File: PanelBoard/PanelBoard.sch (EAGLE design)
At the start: 8 parts, among them K1 ARK500/2, K2 ARK500/2, K3 ARK500/2, K4 ARK500/2

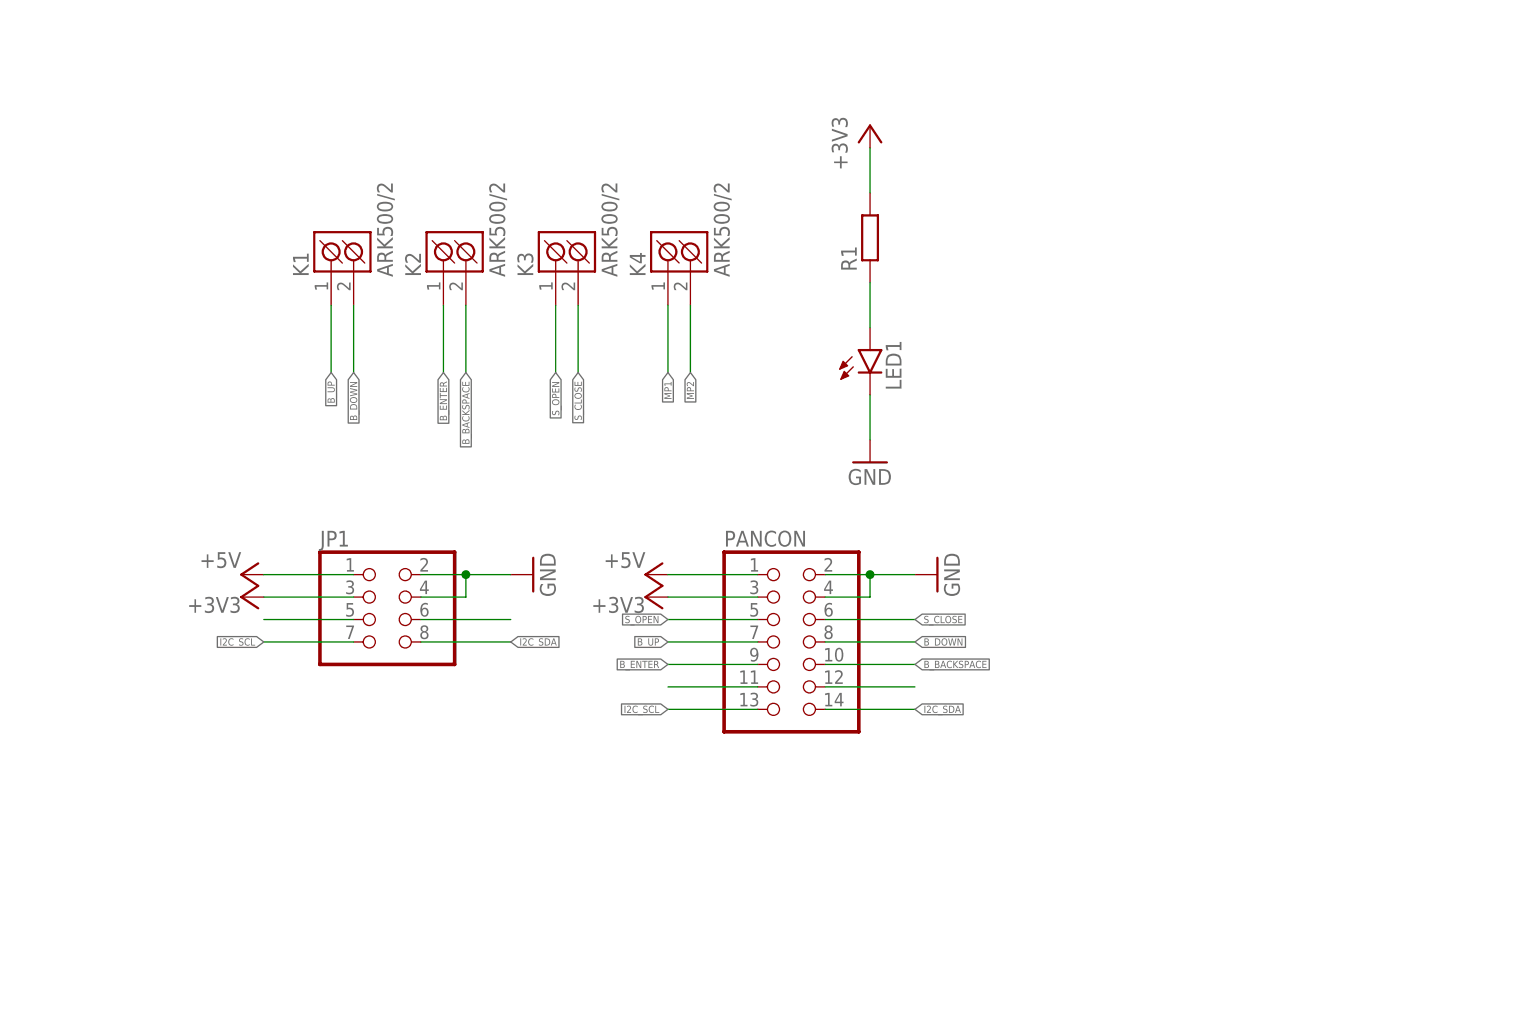
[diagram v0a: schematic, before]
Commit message: PanelBoard layout reworked
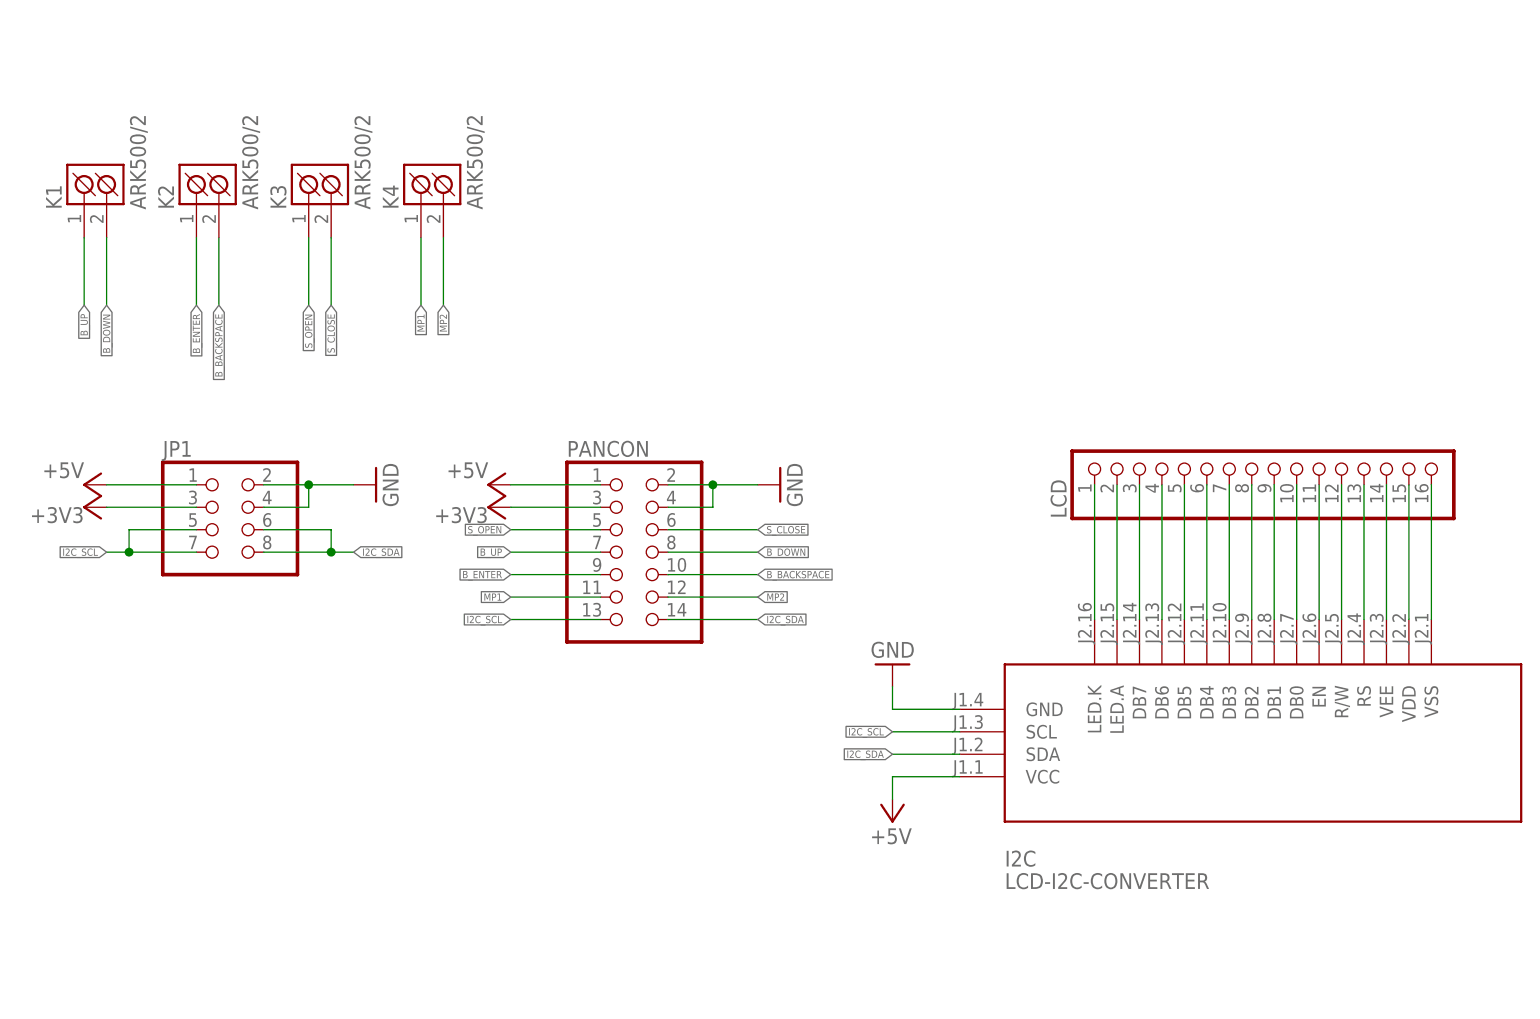
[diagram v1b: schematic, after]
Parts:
- removed LED1: (no value), led:LEDCHIPLED_0603
- removed R1: (no value), rcl:R-EU_R0603
- added I2C: LCD-I2C-CONVERTER, diy-modules:LCD-I2C-CONVERTER
- added LCD: (no value), pinhead:PINHD-1X16
- JP1: device pinhead:PINHD-2X4 -> pinhead:PINHD-2X4/90
- PANCON: device pinhead:PINHD-2X7 -> pinhead:PINHD-2X7/90
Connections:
- removed net N$1: JP1.5
- removed net N$2: JP1.6
- removed net N$4: LED1.A, R1.1
- removed net N$8: PANCON.11
- removed net N$9: PANCON.12
- new net N$10: I2C.DB5, LCD.5
- new net N$11: I2C.DB4, LCD.6
- new net N$12: I2C.DB3, LCD.7
- new net N$13: I2C.DB2, LCD.8
- new net N$14: I2C.DB1, LCD.9
- new net N$15: I2C.DB0, LCD.10
- new net N$16: I2C.EN, LCD.11
- new net N$17: I2C.R/W, LCD.12
- new net N$18: I2C.RS, LCD.13
- new net N$19: I2C.VEE, LCD.14
- new net N$20: I2C.VDD, LCD.15
- new net N$21: I2C.VSS, LCD.16
- new net N$3: I2C.LED.K, LCD.1
- new net N$5: I2C.LED.A, LCD.2
- new net N$6: I2C.DB7, LCD.3
- new net N$7: I2C.DB6, LCD.4
- net +3V3: no longer R1.2
- net +5V: now also I2C.VCC
- net GND: now also I2C.GND; no longer LED1.C
- net I2C_SCL: now also I2C.SCL, JP1.5
- net I2C_SDA: now also I2C.SDA, JP1.6
- net MP1: now also PANCON.11
- net MP2: now also PANCON.12
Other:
- moved on the sheet: JP1, K1, K2, K3, K4, PANCON

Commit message: Improved schematics layout.
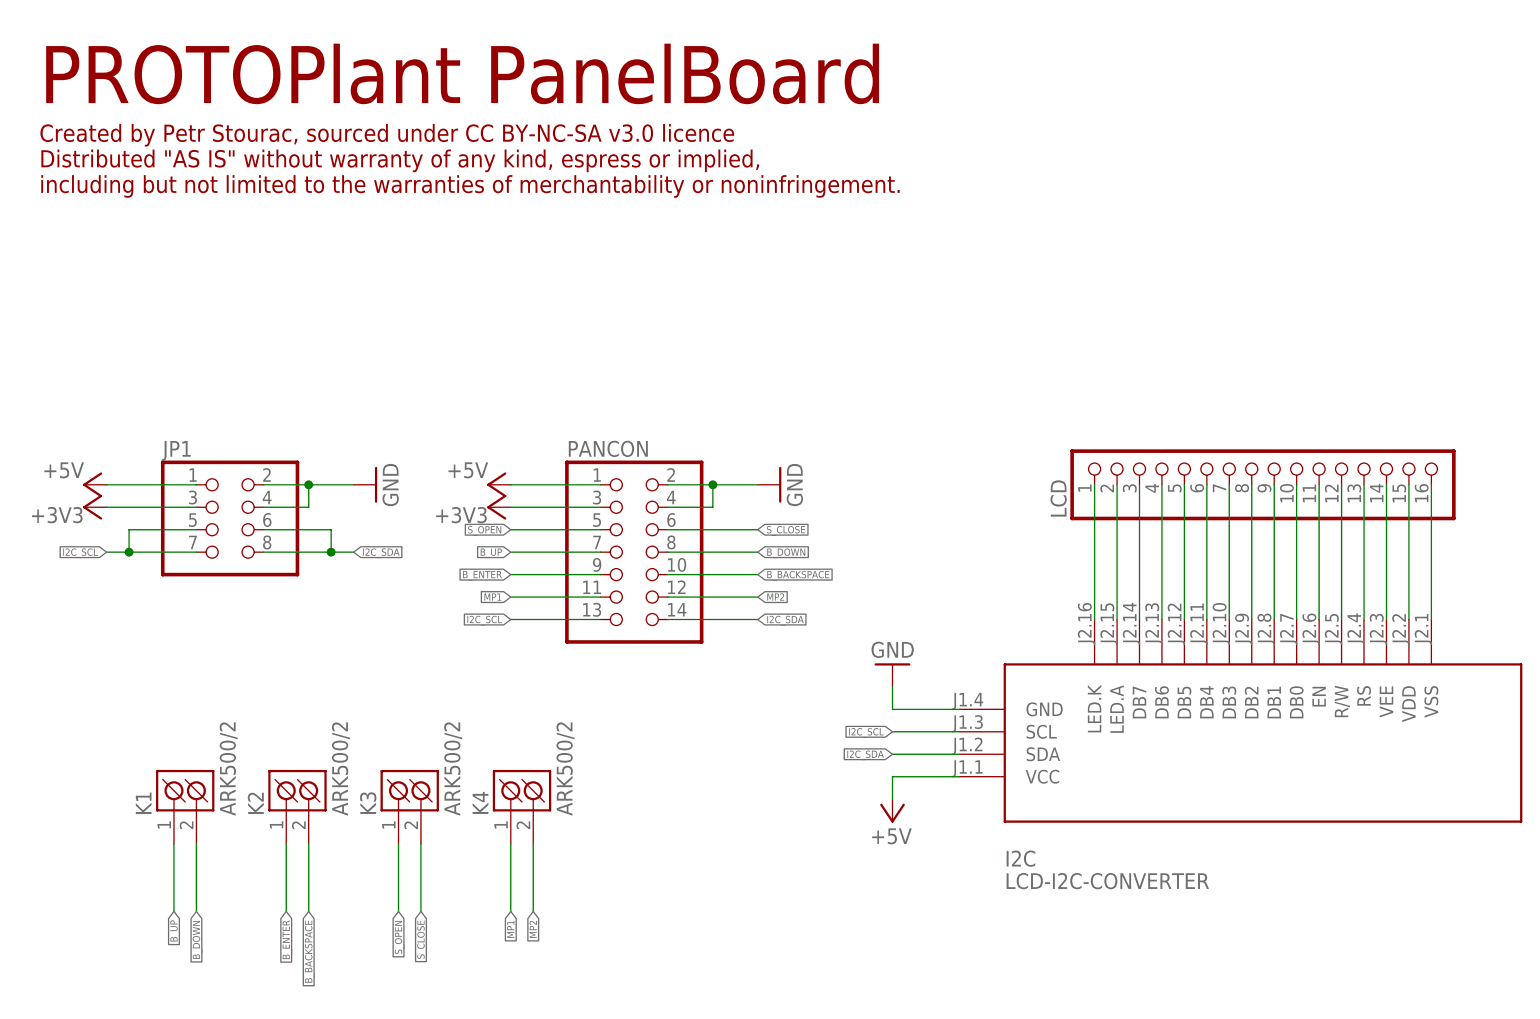
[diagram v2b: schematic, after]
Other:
- note added: "Created by Petr Stourac, sourced under CC BY-NC-SA v3.0 licence Distributed "AS IS" without warranty of any kind, espress or implied, including but not limited to the warranties of merchantability or noninfringement."
- note added: "PROTOPlant PanelBoard"
- moved on the sheet: K1, K2, K3, K4
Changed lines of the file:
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@@
 <?xml version="1.0" encoding="utf-8"?>
 <!DOCTYPE eagle SYSTEM "eagle.dtd">
-<eagle version="9.5.2">
+<eagle version="9.6.1">
 <drawing>
 <settings>
@@
 <setting verticaltext="up"/>
 </settings>
-<grid distance="0.1" unitdist="inch" unit="inch" style="lines" multiple="1" display="no" altdistance="0.01" altunitdist="inch" altunit="inch"/>
+<grid distance="0.1" unitdist="inch" unit="inch" style="lines" multiple="1" display="yes" altdistance="0.01" altunitdist="inch" altunit="inch"/>
 <layers>
 <layer number="1" name="Top" color="4" fill="1" visible="no" active="no"/>
@@
 <parts>
 <part name="FRAME1" library="frames" library_urn="urn:adsk.eagle:library:229" deviceset="A5L-LOC" device=""/>
-<part name="K1" library="#PaJa_konektory" deviceset="ARK500/2" device=""/>
-<part name="K2" library="#PaJa_konektory" deviceset="ARK500/2" device=""/>
-<part name="K3" library="#PaJa_konektory" deviceset="ARK500/2" device=""/>
-<part name="K4" library="#PaJa_konektory" deviceset="ARK500/2" device=""/>
+<part name="K1" library="#PaJa_konektory" library_urn="urn:adsk.eagle:library:19754563" deviceset="ARK500/2" device="" package3d_urn="urn:adsk.eagle:package:19754484/4"/>
+<part name="K2" library="#PaJa_konektory" library_urn="urn:adsk.eagle:library:19754563" deviceset="ARK500/2" device="" package3d_urn="urn:adsk.eagle:package:19754484/4"/>
+<part name="K3" library="#PaJa_konektory" library_urn="urn:adsk.eagle:library:19754563" deviceset="ARK500/2" device="" package3d_urn="urn:adsk.eagle:package:19754484/4"/>
+<part name="K4" library="#PaJa_konektory" library_urn="urn:adsk.eagle:library:19754563" deviceset="ARK500/2" device="" package3d_urn="urn:adsk.eagle:package:19754484/4"/>
 <part name="JP1" library="pinhead" library_urn="urn:adsk.eagle:library:325" deviceset="PINHD-2X4" device="/90" package3d_urn="urn:adsk.eagle:package:22465/2"/>
 <part name="PANCON" library="pinhead" library_urn="urn:adsk.eagle:library:325" deviceset="PINHD-2X7" device="/90" package3d_urn="urn:adsk.eagle:package:22479/2"/>
@@
 <sheet>
 <plain>
+<text x="7.62" y="119.38" size="6.4516" layer="94">PROTOPlant PanelBoard</text>
+<text x="7.62" y="109.22" size="1.9304" layer="94">Created by Petr Stourac, sourced under CC BY-NC-SA v3.0 licence
+Distributed "AS IS" without warranty of any kind, espress or implied,
+including but not limited to the warranties of merchantability or noninfringement.</text>
 </plain>
 <instances>
@@
 <attribute name="SHEET" x="154.305" y="5.08" size="2.54" layer="94"/>
 </instance>
-<instance part="K1" gate="K" x="12.7" y="109.22" smashed="yes" rot="R90">
-<attribute name="NAME" x="10.161" y="107.3335" size="1.778" layer="95" rot="R90"/>
-<attribute name="VALUE" x="19.679" y="107.3335" size="1.778" layer="96" rot="R90"/>
-</instance>
-<instance part="K2" gate="K" x="25.4" y="109.22" smashed="yes" rot="R90">
-<attribute name="NAME" x="22.861" y="107.3335" size="1.778" layer="95" rot="R90"/>
-<attribute name="VALUE" x="32.379" y="107.3335" size="1.778" layer="96" rot="R90"/>
-</instance>
-<instance part="K3" gate="K" x="38.1" y="109.22" smashed="yes" rot="R90">
-<attribute name="NAME" x="35.561" y="107.3335" size="1.778" layer="95" rot="R90"/>
-<attribute name="VALUE" x="45.079" y="107.3335" size="1.778" layer="96" rot="R90"/>
-</instance>
-<instance part="K4" gate="K" x="50.8" y="109.22" smashed="yes" rot="R90">
-<attribute name="NAME" x="48.261" y="107.3335" size="1.778" layer="95" rot="R90"/>
-<attribute name="VALUE" x="57.779" y="107.3335" size="1.778" layer="96" rot="R90"/>
+<instance part="K1" gate="K" x="22.86" y="40.64" smashed="yes" rot="R90">
+<attribute name="NAME" x="20.321" y="38.7535" size="1.778" layer="95" rot="R90"/>
+<attribute name="VALUE" x="29.839" y="38.7535" size="1.778" layer="96" rot="R90"/>
+</instance>
+<instance part="K2" gate="K" x="35.56" y="40.64" smashed="yes" rot="R90">
+<attribute name="NAME" x="33.021" y="38.7535" size="1.778" layer="95" rot="R90"/>
+<attribute name="VALUE" x="42.539" y="38.7535" size="1.778" layer="96" rot="R90"/>
+</instance>
+<instance part="K3" gate="K" x="48.26" y="40.64" smashed="yes" rot="R90">
+<attribute name="NAME" x="45.721" y="38.7535" size="1.778" layer="95" rot="R90"/>
+<attribute name="VALUE" x="55.239" y="38.7535" size="1.778" layer="96" rot="R90"/>
+</instance>
+<instance part="K4" gate="K" x="60.96" y="40.64" smashed="yes" rot="R90">
+<attribute name="NAME" x="58.421" y="38.7535" size="1.778" layer="95" rot="R90"/>
+<attribute name="VALUE" x="67.939" y="38.7535" size="1.778" layer="96" rot="R90"/>
 </instance>
 <instance part="JP1" gate="A" x="27.94" y="71.12" smashed="yes">
@@
 <segment>
 <pinref part="K1" gate="K" pin="K1"/>
-<wire x1="12.7" y1="104.14" x2="12.7" y2="96.52" width="0.1524" layer="91"/>
-<label x="12.7" y="96.52" size="0.8128" layer="95" rot="R270" xref="yes"/>
+<wire x1="22.86" y1="35.56" x2="22.86" y2="27.94" width="0.1524" layer="91"/>
+<label x="22.86" y="27.94" size="0.8128" layer="95" rot="R270" xref="yes"/>
 </segment>
 <segment>
@@
 <segment>
 <pinref part="K1" gate="K" pin="K2"/>
-<wire x1="15.24" y1="104.14" x2="15.24" y2="96.52" width="0.1524" layer="91"/>
-<label x="15.24" y="96.52" size="0.8128" layer="95" rot="R270" xref="yes"/>
+<wire x1="25.4" y1="35.56" x2="25.4" y2="27.94" width="0.1524" layer="91"/>
+<label x="25.4" y="27.94" size="0.8128" layer="95" rot="R270" xref="yes"/>
 </segment>
 <segment>
@@
 <segment>
 <pinref part="K2" gate="K" pin="K1"/>
-<wire x1="25.4" y1="104.14" x2="25.4" y2="96.52" width="0.1524" layer="91"/>
-<label x="25.4" y="96.52" size="0.8128" layer="95" rot="R270" xref="yes"/>
+<wire x1="35.56" y1="35.56" x2="35.56" y2="27.94" width="0.1524" layer="91"/>
+<label x="35.56" y="27.94" size="0.8128" layer="95" rot="R270" xref="yes"/>
 </segment>
 <segment>
@@
 <segment>
 <pinref part="K2" gate="K" pin="K2"/>
-<wire x1="27.94" y1="104.14" x2="27.94" y2="96.52" width="0.1524" layer="91"/>
-<label x="27.94" y="96.52" size="0.8128" layer="95" rot="R270" xref="yes"/>
+<wire x1="38.1" y1="35.56" x2="38.1" y2="27.94" width="0.1524" layer="91"/>
+<label x="38.1" y="27.94" size="0.8128" layer="95" rot="R270" xref="yes"/>
 </segment>
 <segment>
@@
 <segment>
 <pinref part="K3" gate="K" pin="K1"/>
-<wire x1="38.1" y1="104.14" x2="38.1" y2="96.52" width="0.1524" layer="91"/>
-<label x="38.1" y="96.52" size="0.8128" layer="95" rot="R270" xref="yes"/>
+<wire x1="48.26" y1="35.56" x2="48.26" y2="27.94" width="0.1524" layer="91"/>
+<label x="48.26" y="27.94" size="0.8128" layer="95" rot="R270" xref="yes"/>
 </segment>
 <segment>
@@
 <segment>
 <pinref part="K3" gate="K" pin="K2"/>
-<wire x1="40.64" y1="104.14" x2="40.64" y2="96.52" width="0.1524" layer="91"/>
-<label x="40.64" y="96.52" size="0.8128" layer="95" rot="R270" xref="yes"/>
+<wire x1="50.8" y1="35.56" x2="50.8" y2="27.94" width="0.1524" layer="91"/>
+<label x="50.8" y="27.94" size="0.8128" layer="95" rot="R270" xref="yes"/>
 </segment>
 <segment>
@@
 <segment>
 <pinref part="K4" gate="K" pin="K1"/>
-<wire x1="50.8" y1="104.14" x2="50.8" y2="96.52" width="0.1524" layer="91"/>
-<label x="50.8" y="96.52" size="0.8128" layer="95" rot="R270" xref="yes"/>
+<wire x1="60.96" y1="35.56" x2="60.96" y2="27.94" width="0.1524" layer="91"/>
+<label x="60.96" y="27.94" size="0.8128" layer="95" rot="R270" xref="yes"/>
 </segment>
 <segment>
@@
 <segment>
 <pinref part="K4" gate="K" pin="K2"/>
-<wire x1="53.34" y1="104.14" x2="53.34" y2="96.52" width="0.1524" layer="91"/>
-<label x="53.34" y="96.52" size="0.8128" layer="95" rot="R270" xref="yes"/>
+<wire x1="63.5" y1="35.56" x2="63.5" y2="27.94" width="0.1524" layer="91"/>
+<label x="63.5" y="27.94" size="0.8128" layer="95" rot="R270" xref="yes"/>
 </segment>
 <segment>
@@
 </drawing>
 <compatibility>
+<note version="6.3" minversion="6.2.2" severity="warning">
+Since Version 6.2.2 text objects can contain more than one line,
+which will not be processed correctly with this version.
+</note>
 <note version="8.2" severity="warning">
 Since Version 8.2, EAGLE supports online libraries. The ids

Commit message: Update schematics
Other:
- note added: "ver. 1 rev. 0"
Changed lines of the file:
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@@
 Distributed "AS IS" without warranty of any kind, espress or implied,
 including but not limited to the warranties of merchantability or noninfringement.</text>
+<text x="140.97" y="20.32" size="2.54" layer="94">ver. 1 rev. 0</text>
 </plain>
 <instances>
